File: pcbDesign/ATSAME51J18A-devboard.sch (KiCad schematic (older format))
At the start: 22 parts, among them J1 Micro_SD_Card, J10 CAN, J2 BAT, J3 QWIIC, J4 L_PINS, J5 NP_OUT, J6 USB, J7 QSPI, J8 R_PINS, J9 USB4105_REVA, U1 TCAN1051GVDRQ1

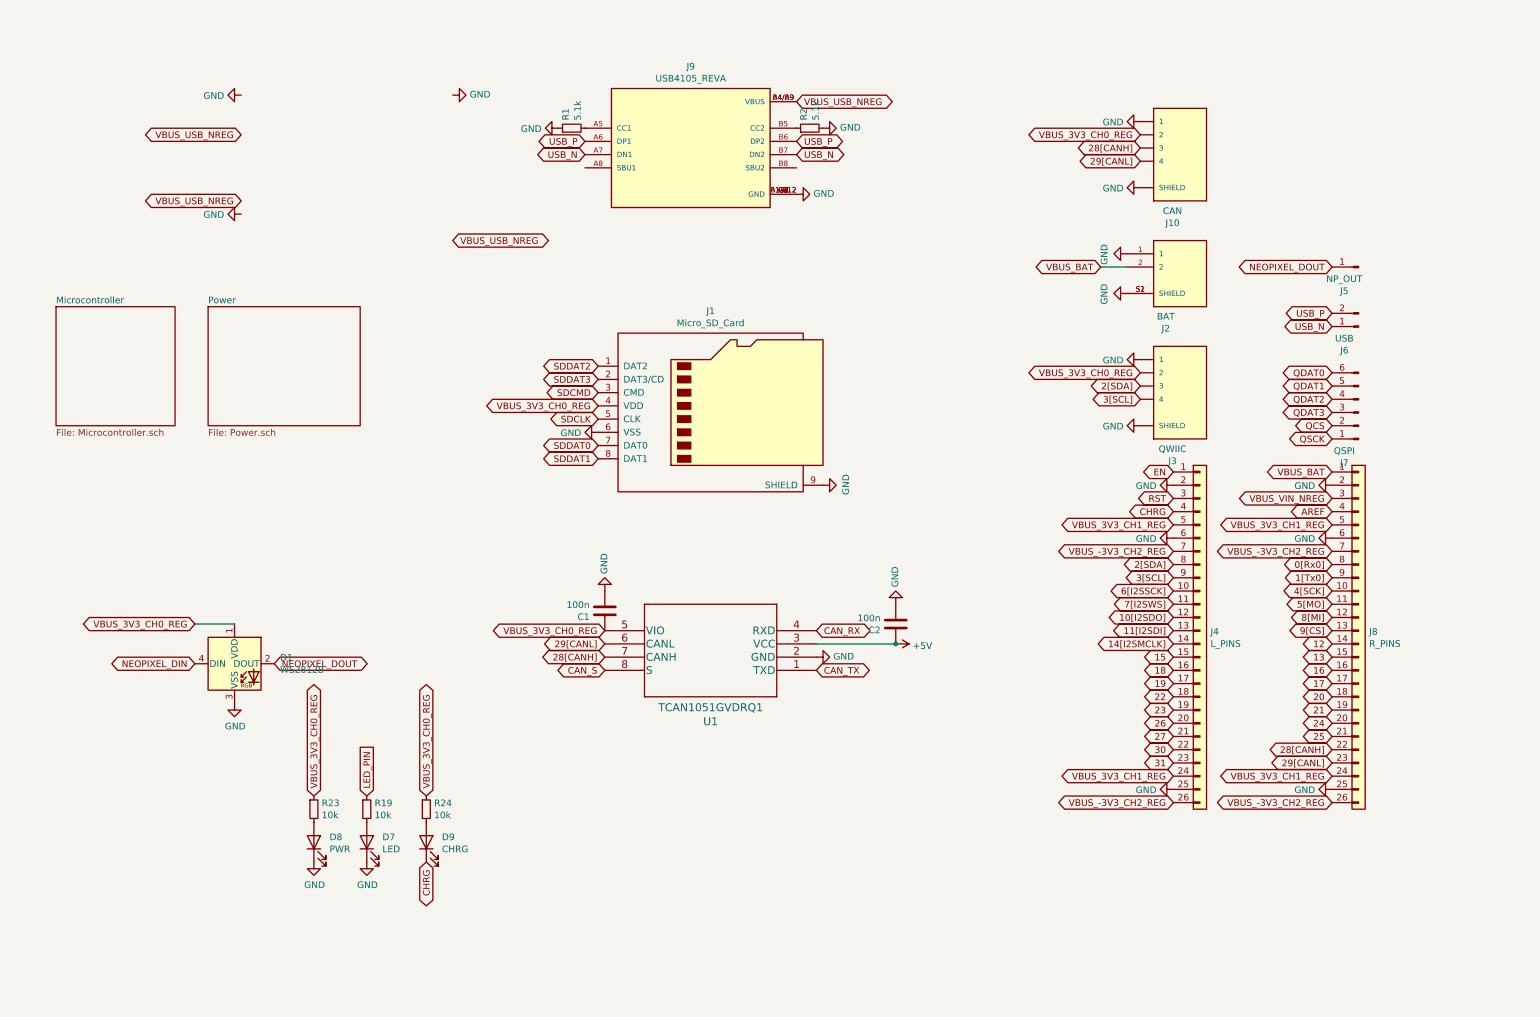
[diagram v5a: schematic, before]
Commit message: Changed the layout of pins to make room for SWD and made the board longer
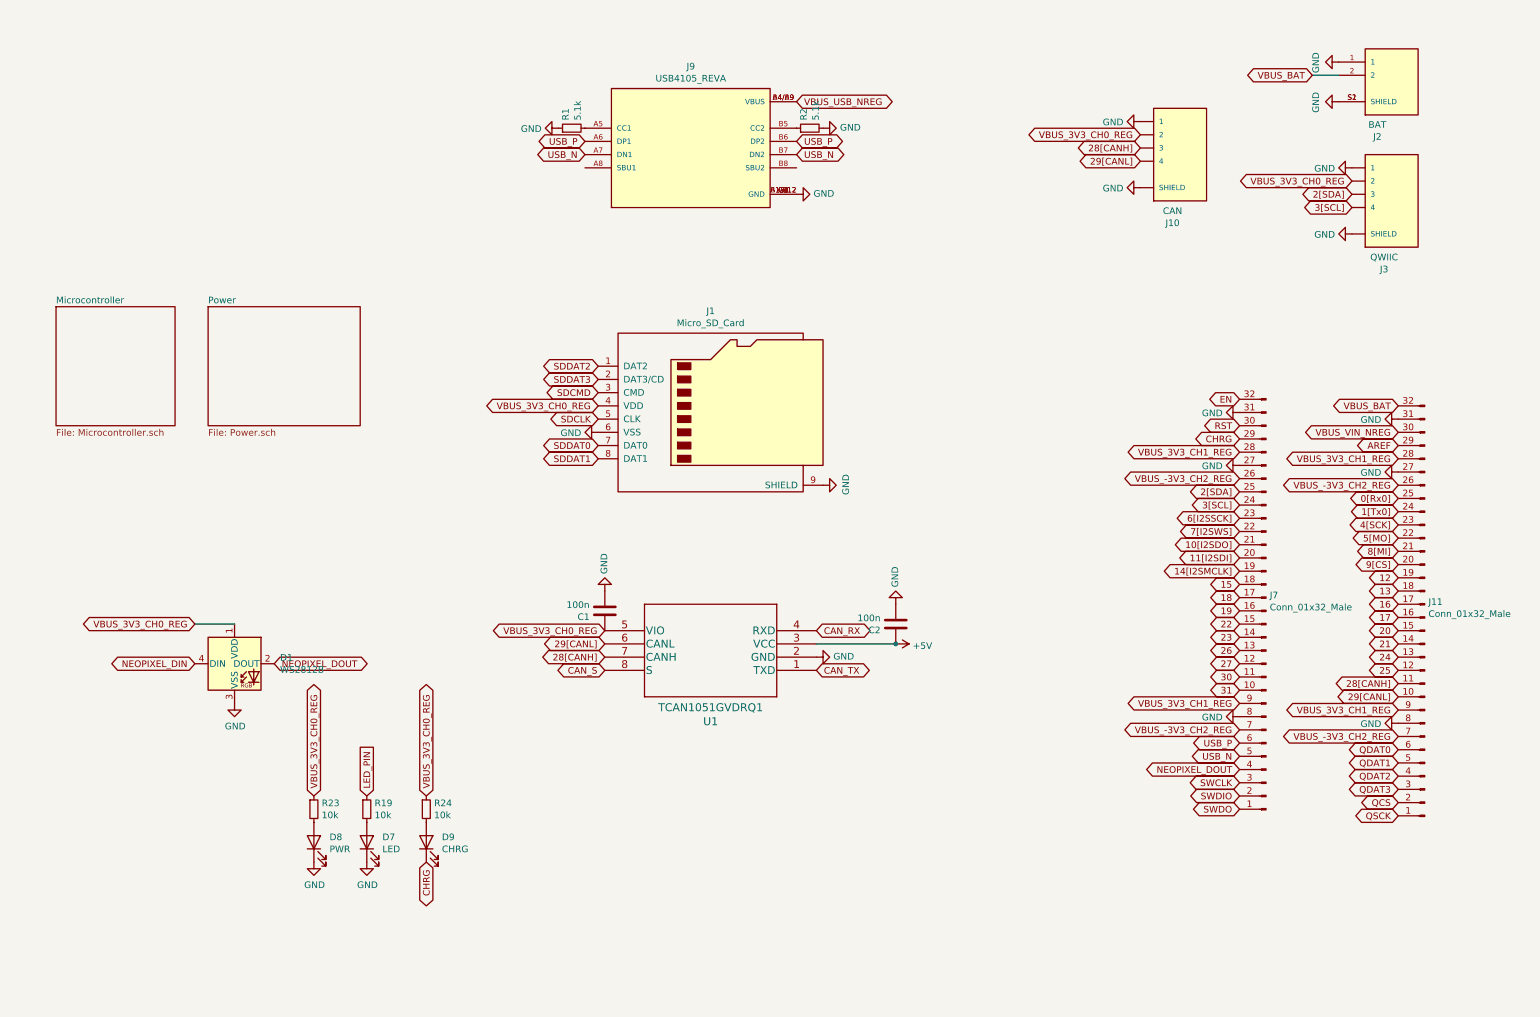
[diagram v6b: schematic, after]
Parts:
- removed J4: L_PINS, Connector_PinSocket_2.54mm:PinSocket_1x26_P2.54mm_Vertical, symbol Connector_Generic:Conn_01x26
- removed J5: NP_OUT, Connector_PinSocket_2.54mm:PinSocket_1x01_P2.54mm_Vertical, symbol Connector:Conn_01x01_Male
- removed J6: USB, Connector_PinSocket_2.54mm:PinSocket_1x02_P2.54mm_Vertical, symbol Connector:Conn_01x02_Male
- removed J7: QSPI, Connector_PinSocket_2.54mm:PinSocket_1x06_P2.54mm_Vertical, symbol Connector:Conn_01x06_Male
- removed J8: R_PINS, Connector_PinSocket_2.54mm:PinSocket_1x26_P2.54mm_Vertical, symbol Connector_Generic:Conn_01x26
- added J11, J7: Conn_01x32_Male, Connector_PinSocket_2.54mm:PinSocket_1x32_P2.54mm_Vertical, symbol Connector:Conn_01x32_Male
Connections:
- net 0[Rx0]: now also J11.25 (Pin_25)
- net 10[I2SDO]: now also J7.21 (Pin_21)
- net 11[I2SDI]: now also J7.20 (Pin_20)
- net 12: now also J11.19 (Pin_19)
- net 13: now also J11.18 (Pin_18)
- net 14[I2SMCLK]: now also J7.19 (Pin_19)
- net 15: now also J7.18 (Pin_18)
- net 16: now also J11.17 (Pin_17)
- net 17: now also J11.16 (Pin_16)
- net 18: now also J7.17 (Pin_17)
- net 19: now also J7.16 (Pin_16)
- net 1[Tx0]: now also J11.24 (Pin_24)
- net 20: now also J11.15 (Pin_15)
- net 21: now also J11.14 (Pin_14)
- net 22: now also J7.15 (Pin_15)
- net 23: now also J7.14 (Pin_14)
- net 24: now also J11.13 (Pin_13)
- net 25: now also J11.12 (Pin_12)
- net 26: now also J7.13 (Pin_13)
- net 27: now also J7.12 (Pin_12)
- net 28[CANH]: now also J11.11 (Pin_11)
- net 29[CANL]: now also J11.10 (Pin_10)
- net 2[SDA]: now also J7.25 (Pin_25)
- net 30: now also J7.11 (Pin_11)
- net 31: now also J7.10 (Pin_10)
- net 3[SCL]: now also J7.24 (Pin_24)
- net 4[SCK]: now also J11.23 (Pin_23)
- net 5[MO]: now also J11.22 (Pin_22)
- net 6[I2SSCK]: now also J7.23 (Pin_23)
- net 7[I2SWS]: now also J7.22 (Pin_22)
- net 8[MI]: now also J11.21 (Pin_21)
- net 9[CS]: now also J11.20 (Pin_20)
- net AREF: now also J11.29 (Pin_29)
- net CHRG: now also J7.29 (Pin_29)
- net EN: now also J7.32 (Pin_32)
- net GND: now also J11.27 (Pin_27), J11.31 (Pin_31), J11.8 (Pin_8), J7.27 (Pin_27), J7.31 (Pin_31), J7.8 (Pin_8)
- net NEOPIXEL_DOUT: now also J7.4 (Pin_4)
- net QCS: now also J11.2 (Pin_2)
- net QDAT0: now also J11.6 (Pin_6)
- net QDAT1: now also J11.5 (Pin_5)
- net QDAT2: now also J11.4 (Pin_4)
- net QDAT3: now also J11.3 (Pin_3)
- net QSCK: now also J11.1 (Pin_1)
- net RST: now also J7.30 (Pin_30)
- net USB_N: now also J7.5 (Pin_5)
- net USB_P: now also J7.6 (Pin_6)
- net VBUS_-3V3_CH2_REG: now also J11.26 (Pin_26), J11.7 (Pin_7), J7.26 (Pin_26), J7.7 (Pin_7)
- net VBUS_3V3_CH1_REG: now also J11.28 (Pin_28), J11.9 (Pin_9), J7.28 (Pin_28), J7.9 (Pin_9)
- net VBUS_BAT: now also J11.32 (Pin_32)
- net VBUS_VIN_NREG: now also J11.30 (Pin_30)
- new net SWCLK: J7.3 (Pin_3)
- new net SWDIO: J7.2 (Pin_2)
- new net SWDO: J7.1 (Pin_1)
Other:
- moved on the sheet: J2, J3

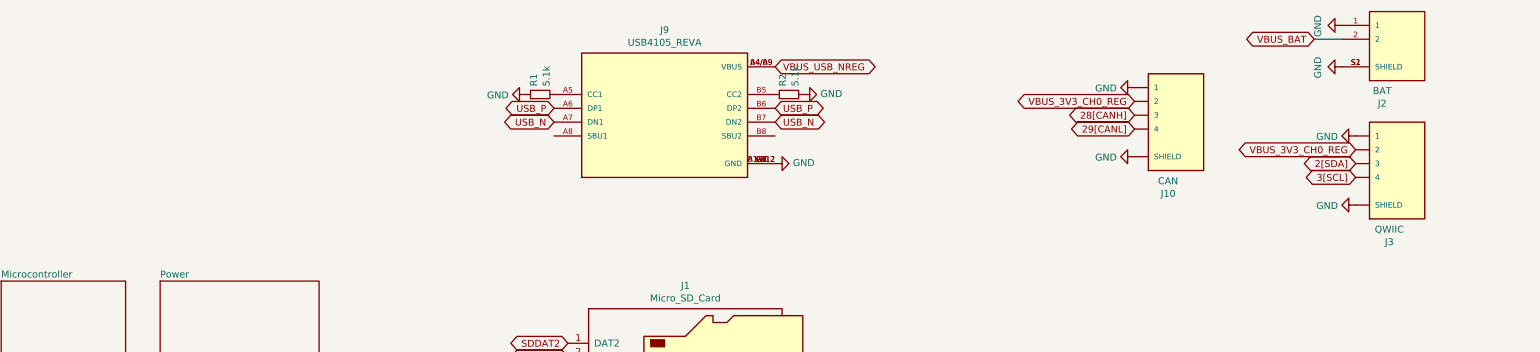
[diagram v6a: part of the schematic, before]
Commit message: Swapped components for more avaiable ones
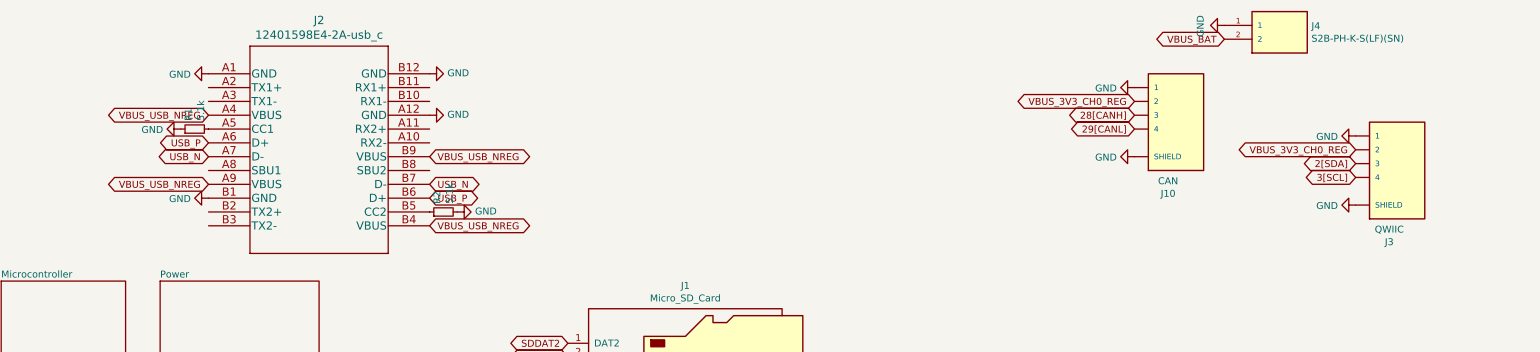
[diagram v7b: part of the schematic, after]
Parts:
- removed J2: BAT, S2B-ZR-SM4A-TF_LF__SN_:JST_S2B-ZR-SM4A-TF(LF)(SN), symbol S2B-ZR-SM4A-TF_LF__SN_:S2B-ZR-SM4A-TF(LF)(SN)
- removed J9: USB4105_REVA, USB4105_REVA:GCT_USB4105_REVA, symbol USB4105_REVA:USB4105_REVA
- added J2: 12401598E4-2A-usb_c, usb_c:12401598E4-2A, symbol ATSAME51J18A-devboard-rescue:12401598E4-2A-usb_c
- added J4: S2B-PH-K-S(LF)(SN), S2B-PH-K-S_LF__SN_:JST_S2B-PH-K-S(LF)(SN), symbol S2B-PH-K-S_LF__SN_:S2B-PH-K-S(LF)(SN)
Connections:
- net GND: now also J2.A1 (GND), J2.A12 (GND), J2.B1 (GND), J2.B12 (GND), J4.1
- net USB_N: now also J2.A7 (D-), J2.B7 (D-)
- net USB_P: now also J2.A6 (D+), J2.B6 (D+)
- net VBUS_BAT: now also J4.2
- net VBUS_USB_NREG: now also J2.A4 (VBUS), J2.A9 (VBUS), J2.B4 (VBUS), J2.B9 (VBUS)
- net at R1.2: now also J2.A5 (CC1)
- net at R2.1: now also J2.B5 (CC2)
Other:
- moved on the sheet: R1, R2
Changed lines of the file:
@@
 Comment4 ""
 $EndDescr
-Text GLabel 4800 1300 0    50   BiDi ~ 0
+Text GLabel 3900 1950 2    50   BiDi ~ 0
 USB_P
 $Comp
@@
 3[SCL]
 $Comp
-L S2B-ZR-SM4A-TF_LF__SN_:S2B-ZR-SM4A-TF(LF)(SN) J2
-U 1 1 606864FC
-P 10900 900
-F 0 "J2" H 10792 535 50  0000 C CNN
-F 1 "BAT" H 10792 626 50  0000 C CNN
-F 2 "S2B-ZR-SM4A-TF_LF__SN_:JST_S2B-ZR-SM4A-TF(LF)(SN)" H 10900 900 50  0001 L BNN
-F 3 "" H 10900 900 50  0001 L BNN
-F 4 "N/A" H 10900 900 50  0001 L BNN "PARTREV"
-F 5 "JST" H 10900 900 50  0001 L BNN "MF"
-F 6 "Manufacturer Recommendations" H 10900 900 50  0001 L BNN "STANDARD"
-	1    10900 900
-	1    0    0    -1
-$EndComp
-$Comp
-L power:GND #PWR05
-U 1 1 60692CD8
-P 10500 1000
-F 0 "#PWR05" H 10500 750 50  0001 C CNN
-F 1 "GND" H 10505 827 50  0000 C CNN
-F 2 "" H 10500 1000 50  0001 C CNN
-F 3 "" H 10500 1000 50  0001 C CNN
-	1    10500 1000
-	0    1    1    0
-$EndComp
-$Comp
 L power:GND #PWR04
 U 1 1 60693F66
-P 10500 700
-F 0 "#PWR04" H 10500 450 50  0001 C CNN
-F 1 "GND" H 10505 527 50  0000 C CNN
-F 2 "" H 10500 700 50  0001 C CNN
-F 3 "" H 10500 700 50  0001 C CNN
-	1    10500 700
-	0    1    1    0
-$EndComp
-Text GLabel 10300 800  0    50   BiDi ~ 0
+P 9650 700
+F 0 "#PWR04" H 9650 450 50  0001 C CNN
+F 1 "GND" H 9655 527 50  0000 C CNN
+F 2 "" H 9650 700 50  0001 C CNN
+F 3 "" H 9650 700 50  0001 C CNN
+	1    9650 700
+	0    1    1    0
+$EndComp
+Text GLabel 9650 800  0    50   BiDi ~ 0
 VBUS_BAT
-Wire Wire Line
-	10300 800  10500 800
 $Sheet
 S 800  2550 900  900
@@
 L Device:R_Small R2
 U 1 1 6060BD83
-P 6500 1200
-F 0 "R2" H 6559 1246 50  0000 L CNN
-F 1 "5.1k" H 6559 1155 50  0000 L CNN
-F 2 "Resistor_SMD:R_0402_1005Metric" H 6500 1200 50  0001 C CNN
-F 3 "~" H 6500 1200 50  0001 C CNN
-	1    6500 1200
+P 4000 2050
+F 0 "R2" H 4059 2096 50  0000 L CNN
+F 1 "5.1k" H 4059 2005 50  0000 L CNN
+F 2 "Resistor_SMD:R_0402_1005Metric" H 4000 2050 50  0001 C CNN
+F 3 "~" H 4000 2050 50  0001 C CNN
+	1    4000 2050
 	0    -1   -1   0
 $EndComp
@@
 	1    0    0    -1
 $EndComp
-Text GLabel 6400 1000 2    50   BiDi ~ 0
+Text GLabel 3900 2150 2    50   BiDi ~ 0
 VBUS_USB_NREG
 $Comp
 L power:GND #PWR0103
 U 1 1 6045FB57
-P 6600 1200
-F 0 "#PWR0103" H 6600 950 50  0001 C CNN
-F 1 "GND" V 6605 1072 50  0000 R CNN
-F 2 "" H 6600 1200 50  0001 C CNN
-F 3 "" H 6600 1200 50  0001 C CNN
-	1    6600 1200
+P 4100 2050
+F 0 "#PWR0103" H 4100 1800 50  0001 C CNN
+F 1 "GND" V 4105 1922 50  0000 R CNN
+F 2 "" H 4100 2050 50  0001 C CNN
+F 3 "" H 4100 2050 50  0001 C CNN
+	1    4100 2050
 	0    -1   -1   0
 $EndComp
@@
 L Device:R_Small R1
 U 1 1 60460985
-P 4700 1200
-F 0 "R1" H 4759 1246 50  0000 L CNN
-F 1 "5.1k" H 4759 1155 50  0000 L CNN
-F 2 "Resistor_SMD:R_0402_1005Metric" H 4700 1200 50  0001 C CNN
-F 3 "~" H 4700 1200 50  0001 C CNN
-	1    4700 1200
+P 2200 1450
+F 0 "R1" H 2259 1496 50  0000 L CNN
+F 1 "5.1k" H 2259 1405 50  0000 L CNN
+F 2 "Resistor_SMD:R_0402_1005Metric" H 2200 1450 50  0001 C CNN
+F 3 "~" H 2200 1450 50  0001 C CNN
+	1    2200 1450
 	0    -1   -1   0
 $EndComp
@@
 L power:GND #PWR0105
 U 1 1 604625F2
-P 4600 1200
-F 0 "#PWR0105" H 4600 950 50  0001 C CNN
-F 1 "GND" V 4605 1072 50  0000 R CNN
-F 2 "" H 4600 1200 50  0001 C CNN
-F 3 "" H 4600 1200 50  0001 C CNN
-	1    4600 1200
-	0    1    1    0
-$EndComp
-Text GLabel 6400 1300 2    50   BiDi ~ 0
+P 2100 1450
+F 0 "#PWR0105" H 2100 1200 50  0001 C CNN
+F 1 "GND" V 2105 1322 50  0000 R CNN
+F 2 "" H 2100 1450 50  0001 C CNN
+F 3 "" H 2100 1450 50  0001 C CNN
+	1    2100 1450
+	0    1    1    0
+$EndComp
+Text GLabel 2300 1550 0    50   BiDi ~ 0
 USB_P
-Text GLabel 4800 1400 0    50   BiDi ~ 0
+Text GLabel 3900 1850 2    50   BiDi ~ 0
 USB_N
-Text GLabel 6400 1400 2    50   BiDi ~ 0
+Text GLabel 2300 1650 0    50   BiDi ~ 0
 USB_N
 $Comp
 L power:GND #PWR0106
 U 1 1 60463C59
-P 6400 1700
-F 0 "#PWR0106" H 6400 1450 50  0001 C CNN
-F 1 "GND" V 6405 1572 50  0000 R CNN
-F 2 "" H 6400 1700 50  0001 C CNN
-F 3 "" H 6400 1700 50  0001 C CNN
-	1    6400 1700
+P 3900 1350
+F 0 "#PWR0106" H 3900 1100 50  0001 C CNN
+F 1 "GND" V 3905 1222 50  0000 R CNN
+F 2 "" H 3900 1350 50  0001 C CNN
+F 3 "" H 3900 1350 50  0001 C CNN
+	1    3900 1350
 	0    -1   -1   0
 $EndComp
@@
 $EndComp
 $Comp
-L USB4105_REVA:USB4105_REVA J9
-U 1 1 60574706
-P 5600 1400
-F 0 "J9" H 5600 2067 50  0000 C CNN
-F 1 "USB4105_REVA" H 5600 1976 50  0000 C CNN
-F 2 "USB4105_REVA:GCT_USB4105_REVA" H 5600 1400 50  0001 L BNN
-F 3 "" H 5600 1400 50  0001 L BNN
-F 4 "3.31 mm" H 5600 1400 50  0001 L BNN "MAXIMUM_PACKAGE_HEIGHT"
-F 5 "GCT" H 5600 1400 50  0001 L BNN "MANUFACTURER"
-F 6 "0.2" H 5600 1400 50  0001 L BNN "PARTREV"
-F 7 "Manufacturer Recommendations" H 5600 1400 50  0001 L BNN "STANDARD"
-	1    5600 1400
-	1    0    0    -1
-$EndComp
-$Comp
 L Connector:Conn_01x32_Male J11
 U 1 1 604E2C58
@@
 Text GLabel 9750 6350 0    50   BiDi ~ 0
 SWDO
+$Comp
+L ATSAME51J18A-devboard-rescue:12401598E4-2A-usb_c J2
+U 1 1 605A0AD6
+P 2300 1050
+F 0 "J2" H 3100 1437 60  0000 C CNN
+F 1 "12401598E4-2A-usb_c" H 3100 1331 60  0000 C CNN
+F 2 "usb_c:12401598E4-2A" H 3100 1290 60  0001 C CNN
+F 3 "" H 2300 1050 60  0000 C CNN
+	1    2300 1050
+	1    0    0    -1
+$EndComp
+Text GLabel 3900 1650 2    50   BiDi ~ 0
+VBUS_USB_NREG
+Text GLabel 2300 1850 0    50   BiDi ~ 0
+VBUS_USB_NREG
+Text GLabel 2300 1350 0    50   BiDi ~ 0
+VBUS_USB_NREG
+$Comp
+L power:GND #PWR0108
+U 1 1 605AC95B
+P 3900 1050
+F 0 "#PWR0108" H 3900 800 50  0001 C CNN
+F 1 "GND" V 3905 922 50  0000 R CNN
+F 2 "" H 3900 1050 50  0001 C CNN
+F 3 "" H 3900 1050 50  0001 C CNN
+	1    3900 1050
+	0    -1   -1   0
+$EndComp
+$Comp
+L power:GND #PWR0113
+U 1 1 605ACC28
+P 2300 1050
+F 0 "#PWR0113" H 2300 800 50  0001 C CNN
+F 1 "GND" V 2305 922 50  0000 R CNN
+F 2 "" H 2300 1050 50  0001 C CNN
+F 3 "" H 2300 1050 50  0001 C CNN
+	1    2300 1050
+	0    1    1    0
+$EndComp
+$Comp
+L power:GND #PWR0122
+U 1 1 605AD8EB
+P 2300 1950
+F 0 "#PWR0122" H 2300 1700 50  0001 C CNN
+F 1 "GND" V 2305 1822 50  0000 R CNN
+F 2 "" H 2300 1950 50  0001 C CNN
+F 3 "" H 2300 1950 50  0001 C CNN
+	1    2300 1950
+	0    1    1    0
+$EndComp
+$Comp
+L S2B-PH-K-S_LF__SN_:S2B-PH-K-S(LF)(SN) J4
+U 1 1 605AF826
+P 10050 700
+F 0 "J4" H 10280 696 50  0000 L CNN
+F 1 "S2B-PH-K-S(LF)(SN)" H 10280 605 50  0000 L CNN
+F 2 "S2B-PH-K-S_LF__SN_:JST_S2B-PH-K-S(LF)(SN)" H 10050 700 50  0001 L BNN
+F 3 "" H 10050 700 50  0001 L BNN
+F 4 "None" H 10050 700 50  0001 L BNN "PRICE"
+F 5 "S2B-PH-K-S_LF__SN_" H 10050 700 50  0001 L BNN "MP"
+F 6 "Unavailable" H 10050 700 50  0001 L BNN "AVAILABILITY"
+F 7 "Connector Header Through Hole, Right Angle 2 position" H 10050 700 50  0001 L BNN "DESCRIPTION"
+F 8 "4.8mm" H 10050 700 50  0001 L BNN "MAXIMUM_PACKAGE_HEIGHT"
+F 9 "JST Sales" H 10050 700 50  0001 L BNN "MF"
+F 10 "None" H 10050 700 50  0001 L BNN "PACKAGE"
+	1    10050 700
+	1    0    0    -1
+$EndComp
 $EndSCHEMATC

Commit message: Begun to make changes to the design
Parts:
- J10, J3: symbol SM04B-SRSS-TB_LF__SN_:SM04B-SRSS-TB(LF)(SN) -> ATSAME51J18A-devboard-rescue:SM04B-SRSS-TB(LF)(SN)-SM04B-SRSS-TB_LF__SN_
- J4: symbol S2B-PH-K-S_LF__SN_:S2B-PH-K-S(LF)(SN) -> ATSAME51J18A-devboard-rescue:S2B-PH-K-S(LF)(SN)-S2B-PH-K-S_LF__SN_
- U1: symbol 2021-03-01_16-21-06:TCAN1051GVDRQ1 -> ATSAME51J18A-devboard-rescue:TCAN1051GVDRQ1-2021-03-01_16-21-06
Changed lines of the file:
@@
 $EndComp
 $Comp
-L SM04B-SRSS-TB_LF__SN_:SM04B-SRSS-TB(LF)(SN) J3
+L ATSAME51J18A-devboard-rescue:SM04B-SRSS-TB(LF)(SN)-SM04B-SRSS-TB_LF__SN_ J3
 U 1 1 60622B92
 P 10900 1700
@@
 VBUS_3V3_CH0_REG
 $Comp
-L 2021-03-01_16-21-06:TCAN1051GVDRQ1 U1
+L ATSAME51J18A-devboard-rescue:TCAN1051GVDRQ1-2021-03-01_16-21-06 U1
 U 1 1 60471FF6
 P 6550 5300
@@
 $EndComp
 $Comp
-L SM04B-SRSS-TB_LF__SN_:SM04B-SRSS-TB(LF)(SN) J10
+L ATSAME51J18A-devboard-rescue:SM04B-SRSS-TB(LF)(SN)-SM04B-SRSS-TB_LF__SN_ J10
 U 1 1 604466EE
 P 9300 1350
@@
 $EndComp
 $Comp
-L S2B-PH-K-S_LF__SN_:S2B-PH-K-S(LF)(SN) J4
+L ATSAME51J18A-devboard-rescue:S2B-PH-K-S(LF)(SN)-S2B-PH-K-S_LF__SN_ J4
 U 1 1 605AF826
 P 10050 700
